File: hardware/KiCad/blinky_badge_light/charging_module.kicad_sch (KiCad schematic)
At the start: 15 parts, among them Q1 N-Channel MOSFET, Q3 N-Channel MOSFET, U2 TP4056

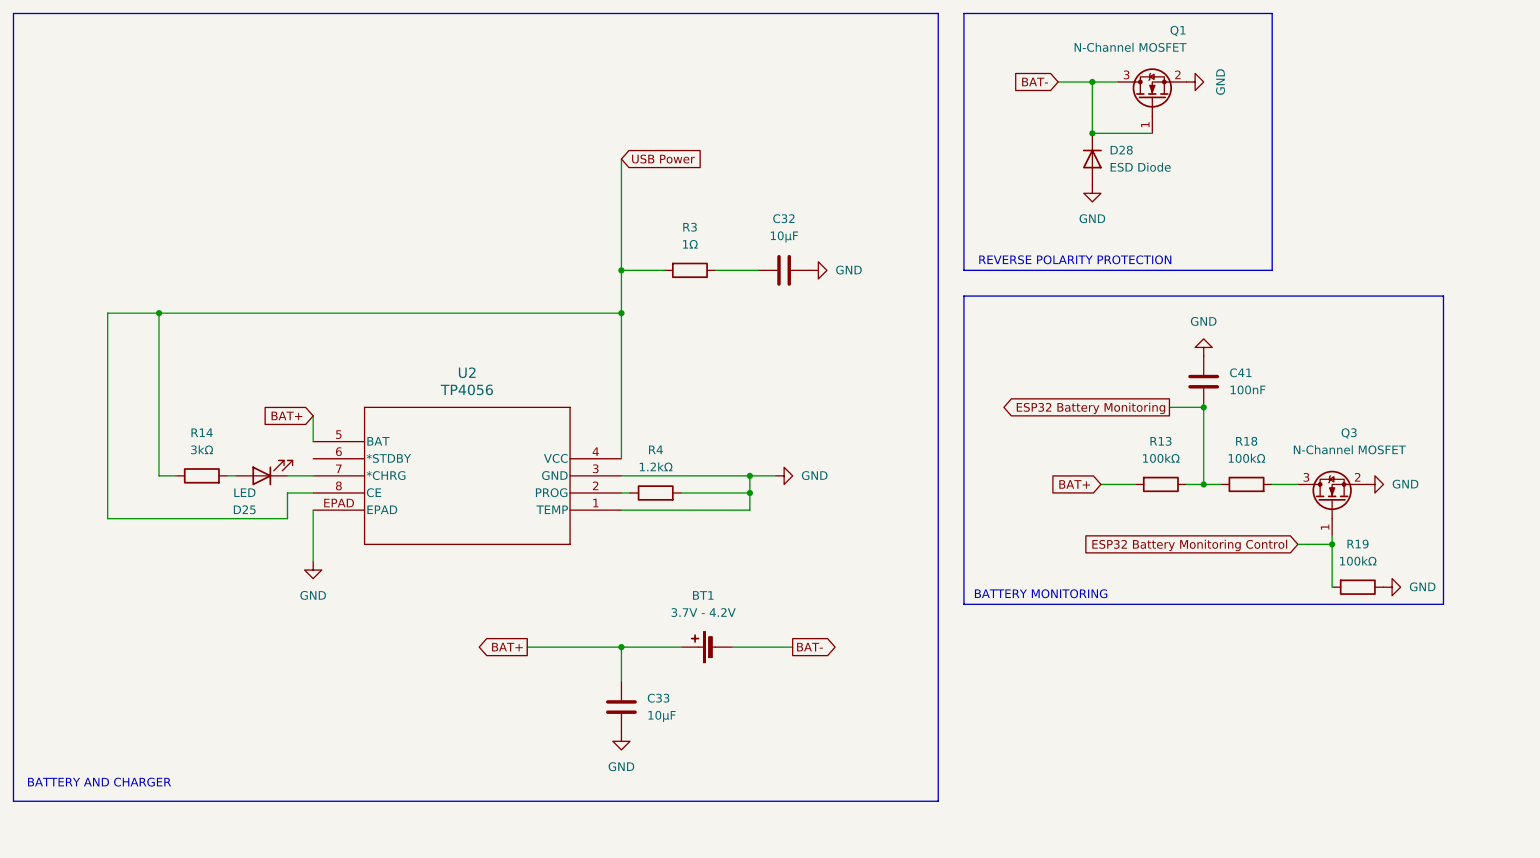
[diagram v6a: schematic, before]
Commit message: adding a bunch of qs and annotated items on schematic
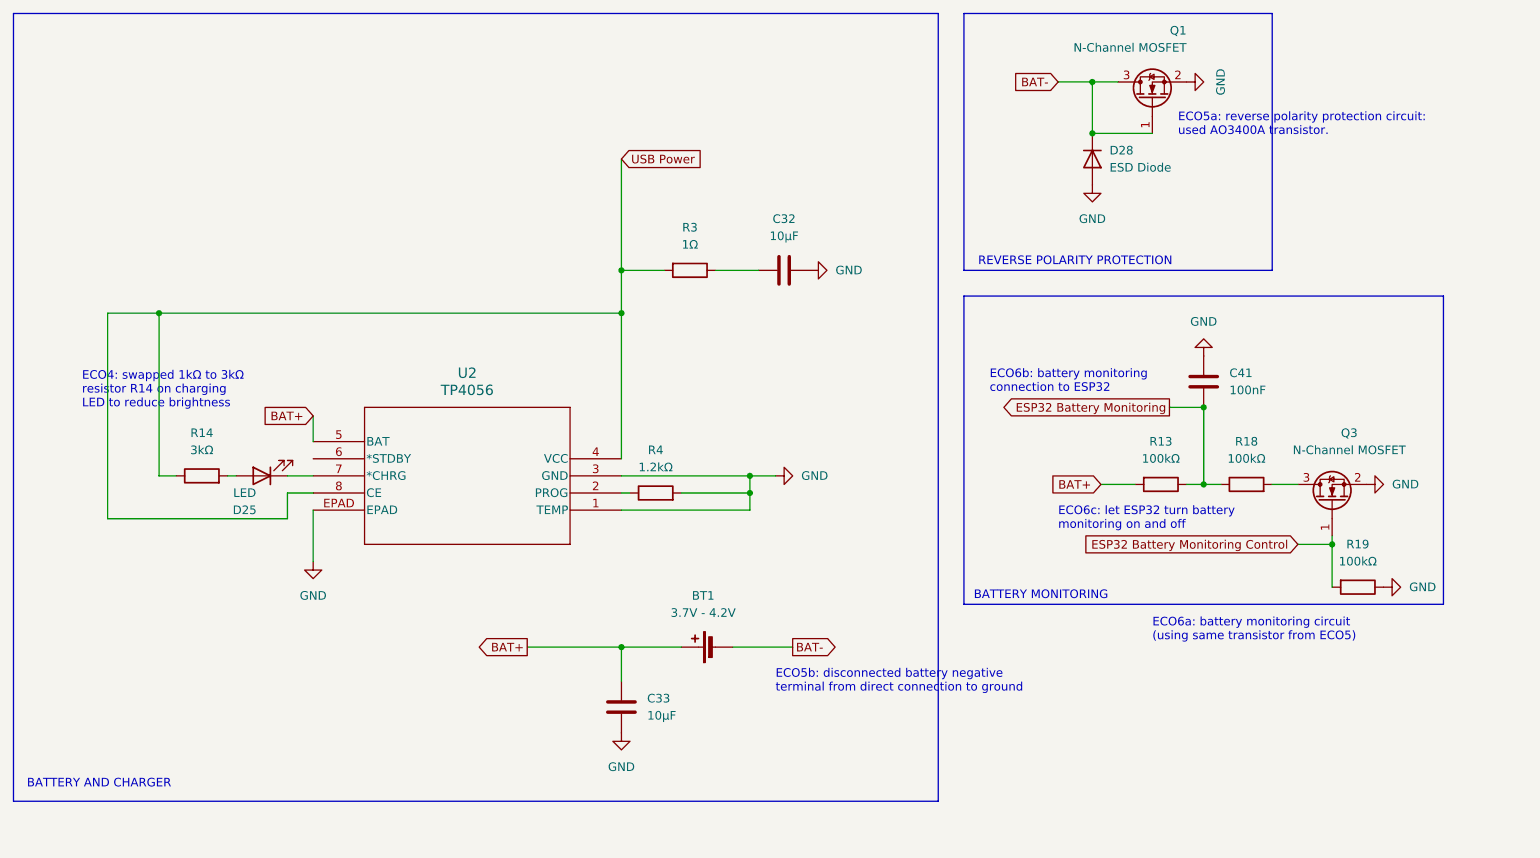
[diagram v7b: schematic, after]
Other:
- note added: "ECO4: swapped 1kΩ to 3kΩ resistor R14 on charging LED to reduce brightness"
- note added: "ECO5a: reverse polarity protection circuit: used AO3400A transistor."
- note added: "ECO5b: disconnected battery negative terminal from direct connection to ground"
- note added: "ECO6a: battery monitoring circuit (using same transistor from ECO5)"
- note added: "ECO6b: battery monitoring connection to ESP32"
- note added: "ECO6c: let ESP32 turn battery monitoring on and off"
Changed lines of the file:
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@@
+		)
+	)
+	(text "ECO5a: reverse polarity protection circuit:\nused AO3400A transistor."
+		(exclude_from_sim yes)
+		(at 189.23 33.02 0)
+		(effects
+			(font
+				(size 1.27 1.27)
+				(color 119 0 255 1)
+			)
+			(justify left)
+		)
+	)
+	(text "ECO5b: disconnected battery negative\nterminal from direct connection to ground"
+		(exclude_from_sim yes)
+		(at 129.54 115.57 0)
+		(effects
+			(font
+				(size 1.27 1.27)
+				(color 119 0 255 1)
+			)
+			(justify left)
+		)
+	)
+	(text "ECO6c: let ESP32 turn battery\nmonitoring on and off"
+		(exclude_from_sim yes)
+		(at 171.45 91.44 0)
+		(effects
+			(font
+				(size 1.27 1.27)
+				(color 119 0 255 1)
+			)
+			(justify left)
+		)
+	)
+	(text "ECO4: swapped 1kΩ to 3kΩ \nresistor R14 on charging \nLED to reduce brightness"
+		(exclude_from_sim yes)
+		(at 26.67 72.39 0)
+		(effects
+			(font
+				(size 1.27 1.27)
+				(color 119 0 255 1)
+			)
+			(justify left)
+		)
+	)
+	(text "ECO6b: battery monitoring\nconnection to ESP32"
+		(exclude_from_sim yes)
+		(at 161.29 71.12 0)
+		(effects
+			(font
+				(size 1.27 1.27)
+				(color 119 0 255 1)
+			)
+			(justify left)
 		)
 	)
@@
 		)
 	)
+	(text "ECO6a: battery monitoring circuit\n(using same transistor from ECO5)"
+		(exclude_from_sim yes)
+		(at 185.42 107.95 0)
+		(effects
+			(font
+				(size 1.27 1.27)
+				(color 119 0 255 1)
+			)
+			(justify left)
+		)
+	)

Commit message: review feedabck
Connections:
- net BAT+: now also D28.1 (K), Q1.1 (G)
- net BAT-: now also D28.2 (A); no longer D28.1 (K), Q1.1 (G)
- net GND: no longer D28.2 (A)
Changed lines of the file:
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@@
 	)
 	(junction
-		(at 176.5206 26.67)
+		(at 176.53 34.29)
 		(diameter 0)
 		(color 0 0 0 0)
@@
 	)
 	(junction
-		(at 176.53 34.29)
-		(diameter 0)
-		(color 0 0 0 0)
-	)
-	(junction
 		(at 193.04 86.36)
 		(diameter 0)
@@
 	(wire
 		(pts
-			(xy 176.53 34.29) (xy 176.5206 34.29)
-		)
-		(stroke
-			(width 0)
-			(type default)
-		)
-	)
-	(wire
-		(pts
 			(xy 38.1 60.96) (xy 106.68 60.96)
 		)
@@
 	(wire
 		(pts
+			(xy 176.53 34.29) (xy 185.42 34.29)
+		)
+		(stroke
+			(width 0)
+			(type default)
+		)
+	)
+	(wire
+		(pts
 			(xy 125.73 85.09) (xy 129.54 85.09)
 		)
@@
 	(wire
 		(pts
+			(xy 168.91 34.29) (xy 176.53 34.29)
+		)
+		(stroke
+			(width 0)
+			(type default)
+		)
+	)
+	(wire
+		(pts
 			(xy 106.68 115.57) (xy 106.68 110.49)
 		)
@@
 	(wire
 		(pts
+			(xy 168.91 41.91) (xy 176.53 41.91)
+		)
+		(stroke
+			(width 0)
+			(type default)
+		)
+	)
+	(wire
+		(pts
 			(xy 92.71 110.49) (xy 106.68 110.49)
 		)
@@
 	(wire
 		(pts
-			(xy 185.42 34.29) (xy 176.53 34.29)
-		)
-		(stroke
-			(width 0)
-			(type default)
-		)
-	)
-	(wire
-		(pts
 			(xy 106.68 87.63) (xy 107.95 87.63)
 		)
@@
 	(wire
 		(pts
-			(xy 171.45 26.67) (xy 176.5206 26.67)
+			(xy 171.45 26.67) (xy 180.34 26.67)
 		)
 		(stroke
@@
 	(wire
 		(pts
-			(xy 176.5206 34.29) (xy 176.5206 26.67)
-		)
-		(stroke
-			(width 0)
-			(type default)
-		)
-	)
-	(wire
-		(pts
 			(xy 106.68 90.17) (xy 125.73 90.17)
 		)
@@
 		(pts
 			(xy 177.8 86.36) (xy 182.88 86.36)
-		)
-		(stroke
-			(width 0)
-			(type default)
-		)
-	)
-	(wire
-		(pts
-			(xy 176.5206 26.67) (xy 180.34 26.67)
 		)
 		(stroke
@@
 		)
 	)
+	(global_label "BAT+"
+		(shape output)
+		(at 168.91 34.29 180)
+		(fields_autoplaced yes)
+		(effects
+			(font
+				(size 1.27 1.27)
+			)
+			(justify right)
+		)
+		(property "Intersheetrefs" "${INTERSHEET_REFS}"
+			(at 161.0262 34.29 0)
+			(effects
+				(font
+					(size 1.27 1.27)
+				)
+				(justify right)
+				(hide yes)
+			)
+		)
+	)
 	(global_label "ESP32 Battery Monitoring"
 		(shape output)
@@
 		(property "Intersheetrefs" "${INTERSHEET_REFS}"
 			(at 171.5497 95.25 0)
+			(effects
+				(font
+					(size 1.27 1.27)
+				)
+				(justify right)
+				(hide yes)
+			)
+		)
+	)
+	(global_label "BAT-"
+		(shape input)
+		(at 168.91 41.91 180)
+		(fields_autoplaced yes)
+		(effects
+			(font
+				(size 1.27 1.27)
+			)
+			(justify right)
+		)
+		(property "Intersheetrefs" "${INTERSHEET_REFS}"
+			(at 161.0262 41.91 0)
 			(effects
 				(font
@@
 					(unit 1)
 				)
-			)
-		)
-	)
-	(symbol
-		(lib_id "power:GND")
-		(at 176.53 41.91 0)
-		(unit 1)
-		(exclude_from_sim no)
-		(in_bom yes)
-		(on_board yes)
-		(dnp no)
-		(fields_autoplaced yes)
-		(property "Reference" "#PWR039"
-			(at 176.53 48.26 0)
-			(effects
-				(font
-					(size 1.27 1.27)
-				)
-				(hide yes)
-			)
-		)
-		(property "Value" "GND"
-			(at 176.53 46.99 0)
-			(effects
-				(font
-					(size 1.27 1.27)
-				)
-			)
-		)
-		(property "Footprint" ""
-			(at 176.53 41.91 0)
-			(effects
-				(font
-					(size 1.27 1.27)
-				)
-				(hide yes)
-			)
-		)
-		(property "Datasheet" ""
-			(at 176.53 41.91 0)
-			(effects
-				(font
-					(size 1.27 1.27)
-				)
-				(hide yes)
-			)
-		)
-		(property "Description" "Power symbol creates a global label with name \"GND\" , ground"
-			(at 176.53 41.91 0)
-			(effects
-				(font
-					(size 1.27 1.27)
-				)
-				(hide yes)
-			)
-		)
-		(pin "1"
-		)
-		(instances
-			(project ""
-				(path "/f33039b1-b38b-4cb6-baf0-07a137773378/ff49f689-50f6-47c9-b665-80ddb7cbc42d"
-					(reference "#PWR039")
-					(unit 1)
-				)
